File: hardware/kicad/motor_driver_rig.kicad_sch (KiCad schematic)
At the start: 8 parts, among them M1 NEMA-17 stepper motor, M2 NEMA-17 stepper motor, M3 NEMA-17 stepper motor, U1 Arduino Uno + CNC Shield V3

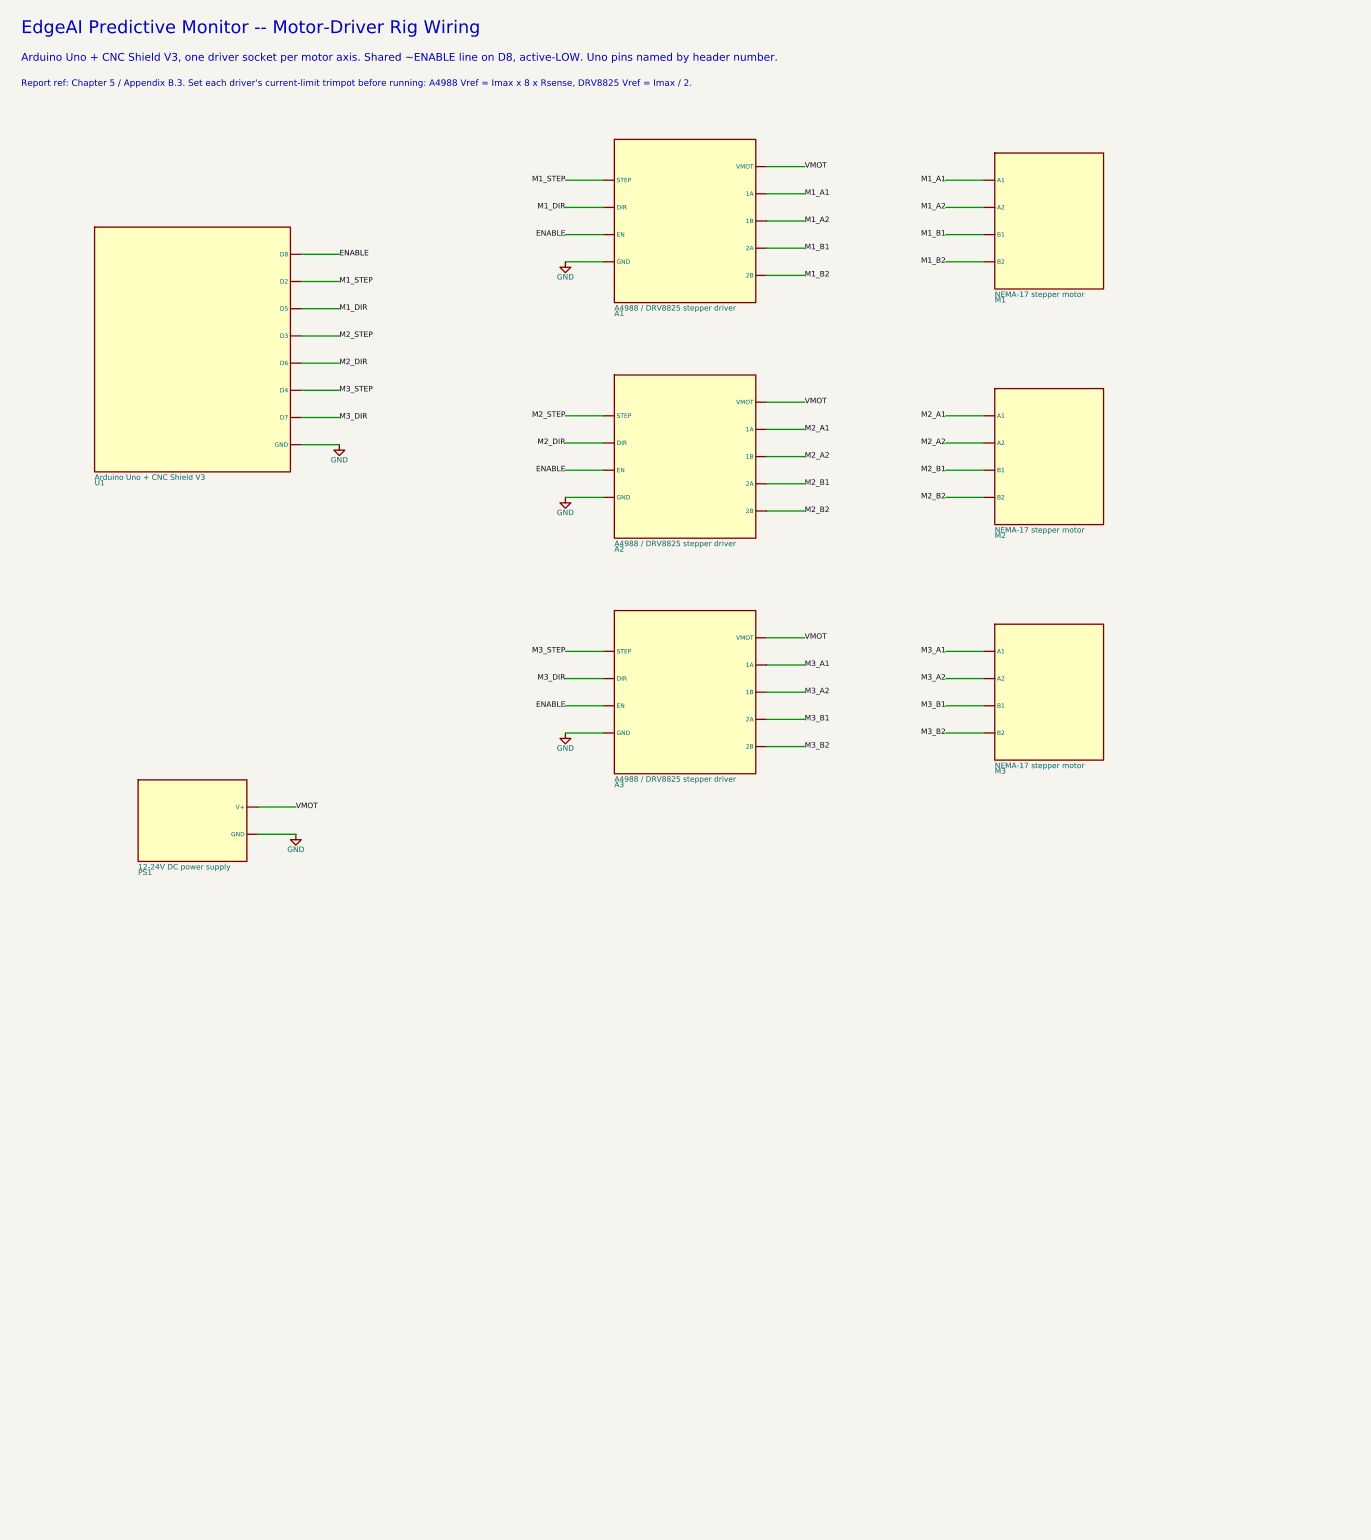
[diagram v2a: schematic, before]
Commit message: schematics: drop report-ref line, enlarge text, tighten crop
The report ref (Chapter/Appendix) was tied to a report structure the
submitted template doesn't use, so it's gone -- the useful pin-naming
and trimpot notes it was bundled with stayed. Separately, headings,
pin names, and net labels were too small to read once pasted into a
Word doc, so all text sizes went up in gen.py; row spacing now derives
from each part's real box height (via a new stack_column() helper)
instead of fixed y-coordinates, since the bigger fonts no longer fit
the old hand-picked positions. Crop step now masks out just the
title-block corner instead of scanning a fixed window, which cuts the
white margin around each exported PNG/PDF down to ~25px.

Co-Authored-By: Claude Sonnet 5 <noreply@anthropic.com>
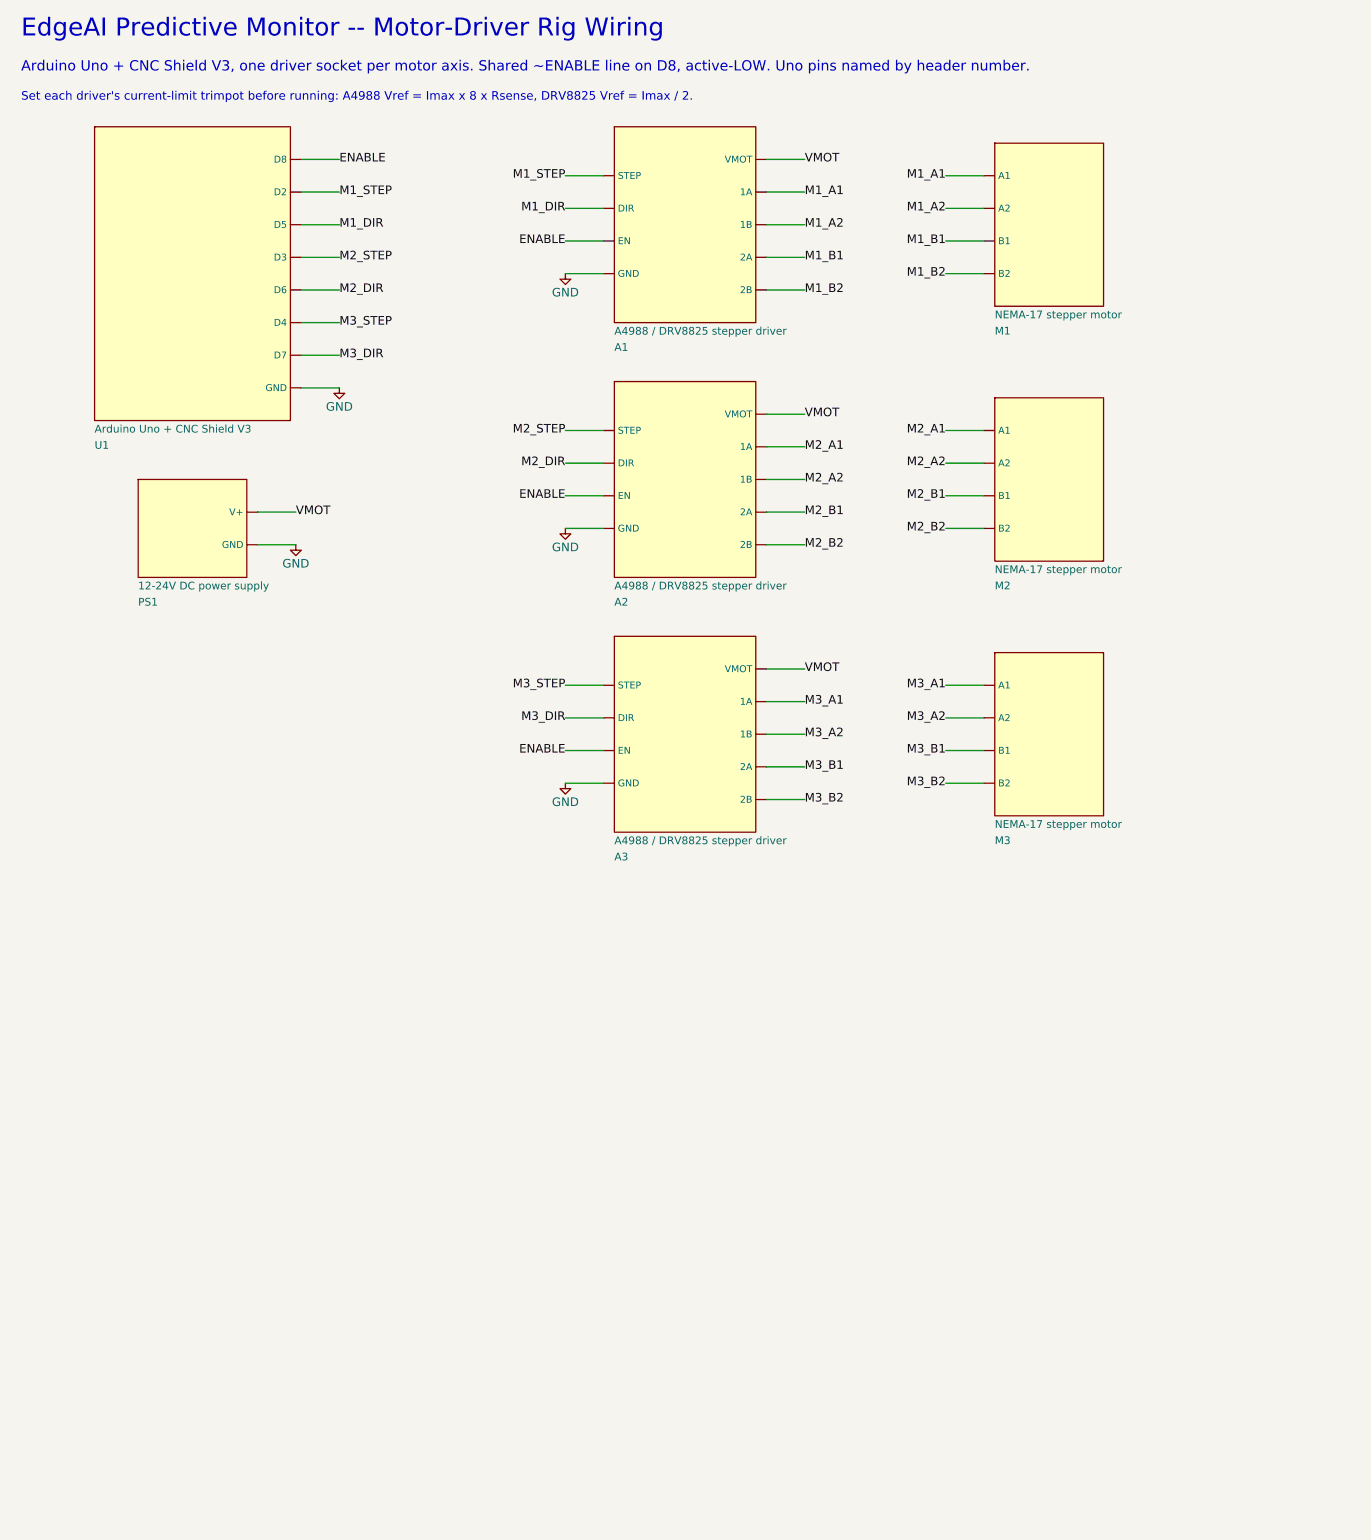
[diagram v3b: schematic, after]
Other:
- note added: "Set each driver's current-limit trimpot before running: A4988 Vref = Imax x 8 x Rsense, DRV8825 Vref = Imax / 2."
- note removed: "Report ref: Chapter 5 / Appendix B.3. Set each driver's current-limit trimpot before running: A4988 Vref = Imax x 8 x Rsense, DRV8825 Vref = Imax / 2."

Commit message: schematics: rework motor-driver rig to 2 columns, shorten subtitle
3 side-by-side columns (hub, driver, motor) squeezed to illegible
when pasted into Word, unlike the other two diagrams which are 2
columns. Driver and motor are now stacked per axis in a single right
column instead -- connectivity is unaffected since this style already
wires everything by matching net labels, not physical adjacency.
Also trimmed the subtitle, which at 134 chars had become the widest
line on the sheet and was stretching the crop past the actual circuit.

Co-Authored-By: Claude Sonnet 5 <noreply@anthropic.com>
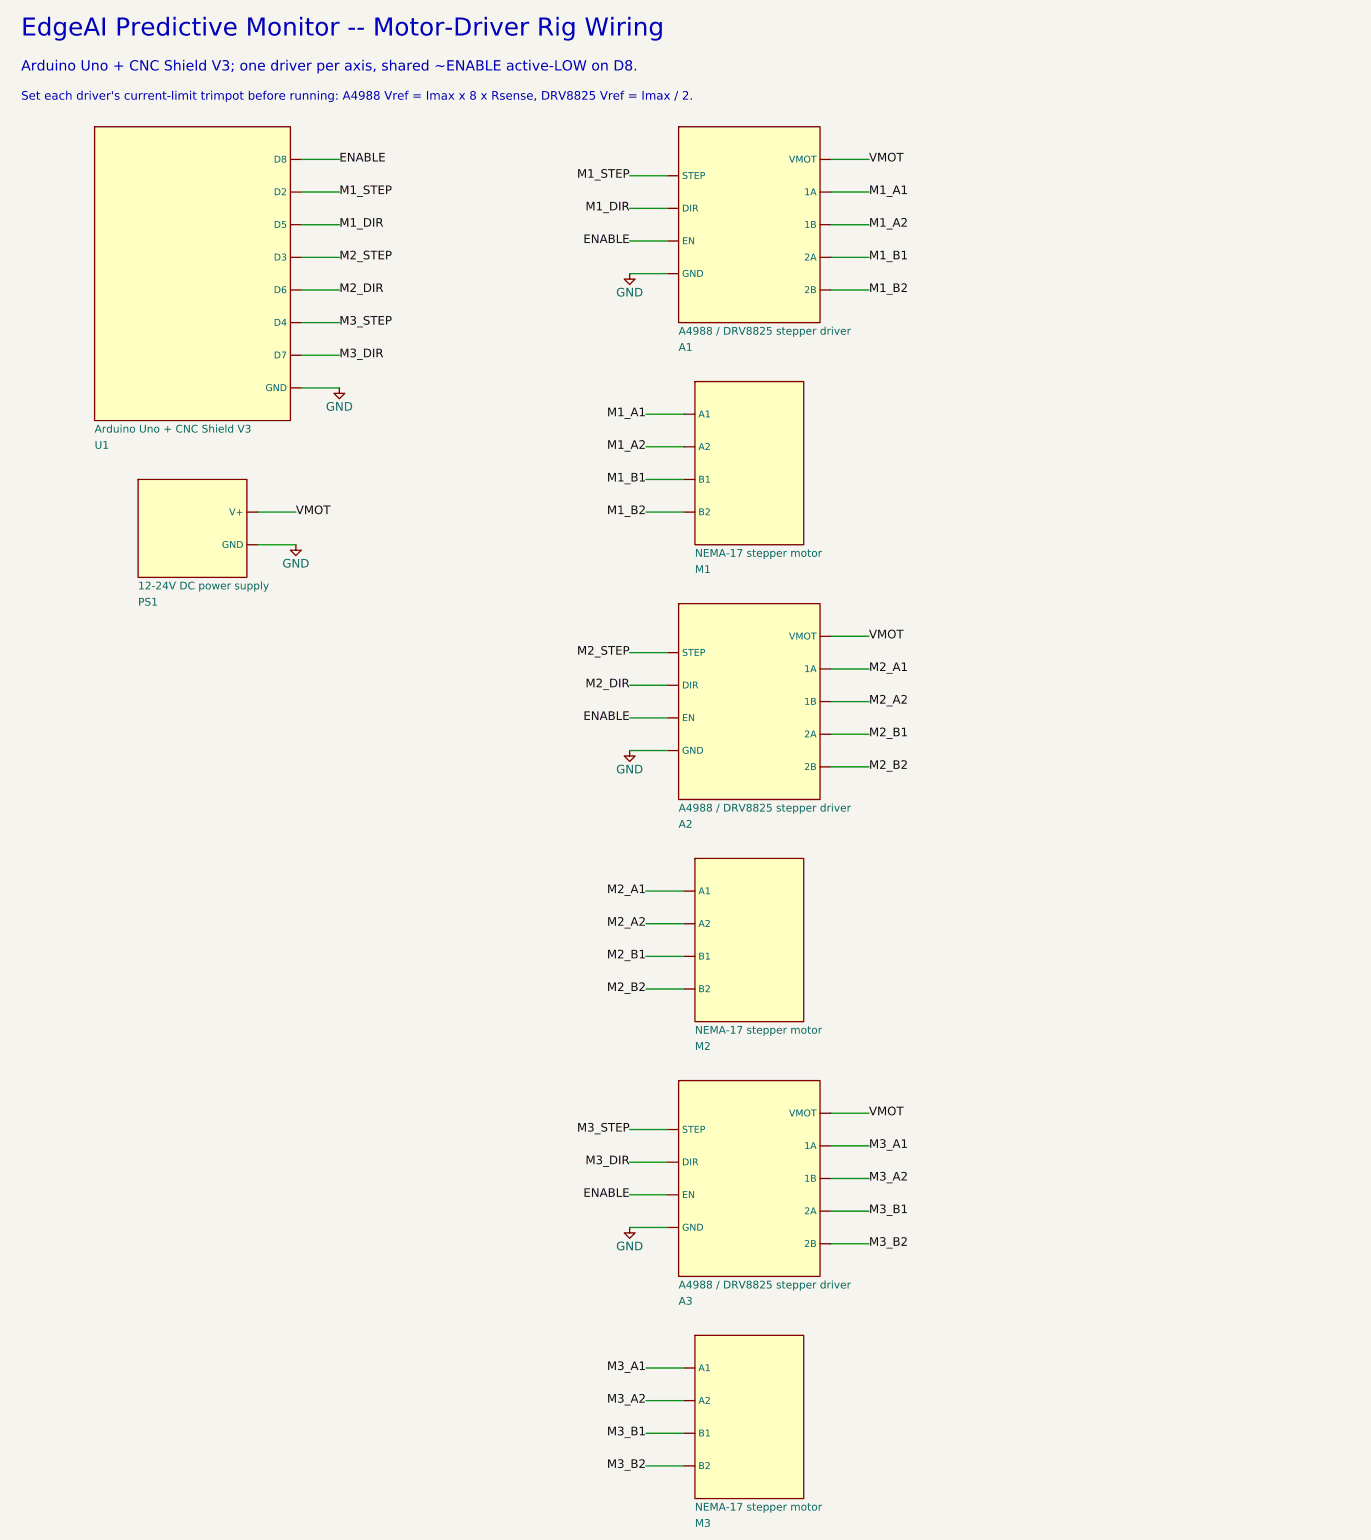
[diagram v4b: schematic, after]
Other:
- note added: "Arduino Uno + CNC Shield V3; one driver per axis, shared ~ENABLE active-LOW on D8."
- note removed: "Arduino Uno + CNC Shield V3, one driver socket per motor axis. Shared ~ENABLE line on D8, active-LOW. Uno pins named by header number."

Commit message: schematics: fix motor-driver rig layout to fill both columns, bottom cutoff
The previous 2-column pass stacked driver+motor per axis in a single
tall right column while the left column (hub+PSU) sat mostly empty --
6 rows deep, it also overflowed the A3 sheet height and got the M2/M3
row silently clipped by kicad-cli's page-bound raster export.

Now both columns carry rows: Uno + PSU share row 1, then each axis's
driver (col 1) and motor (col 2) share a row -- 4 rows instead of 6,
both columns filled, driver/motor labels still face each other across
the gap. Bumped the sheet to A2 for headroom against the same overflow
next time a part or row count grows; the auto-crop keeps the exported
image sized to content regardless, so this adds no visible whitespace.

Co-Authored-By: Claude Sonnet 5 <noreply@anthropic.com>
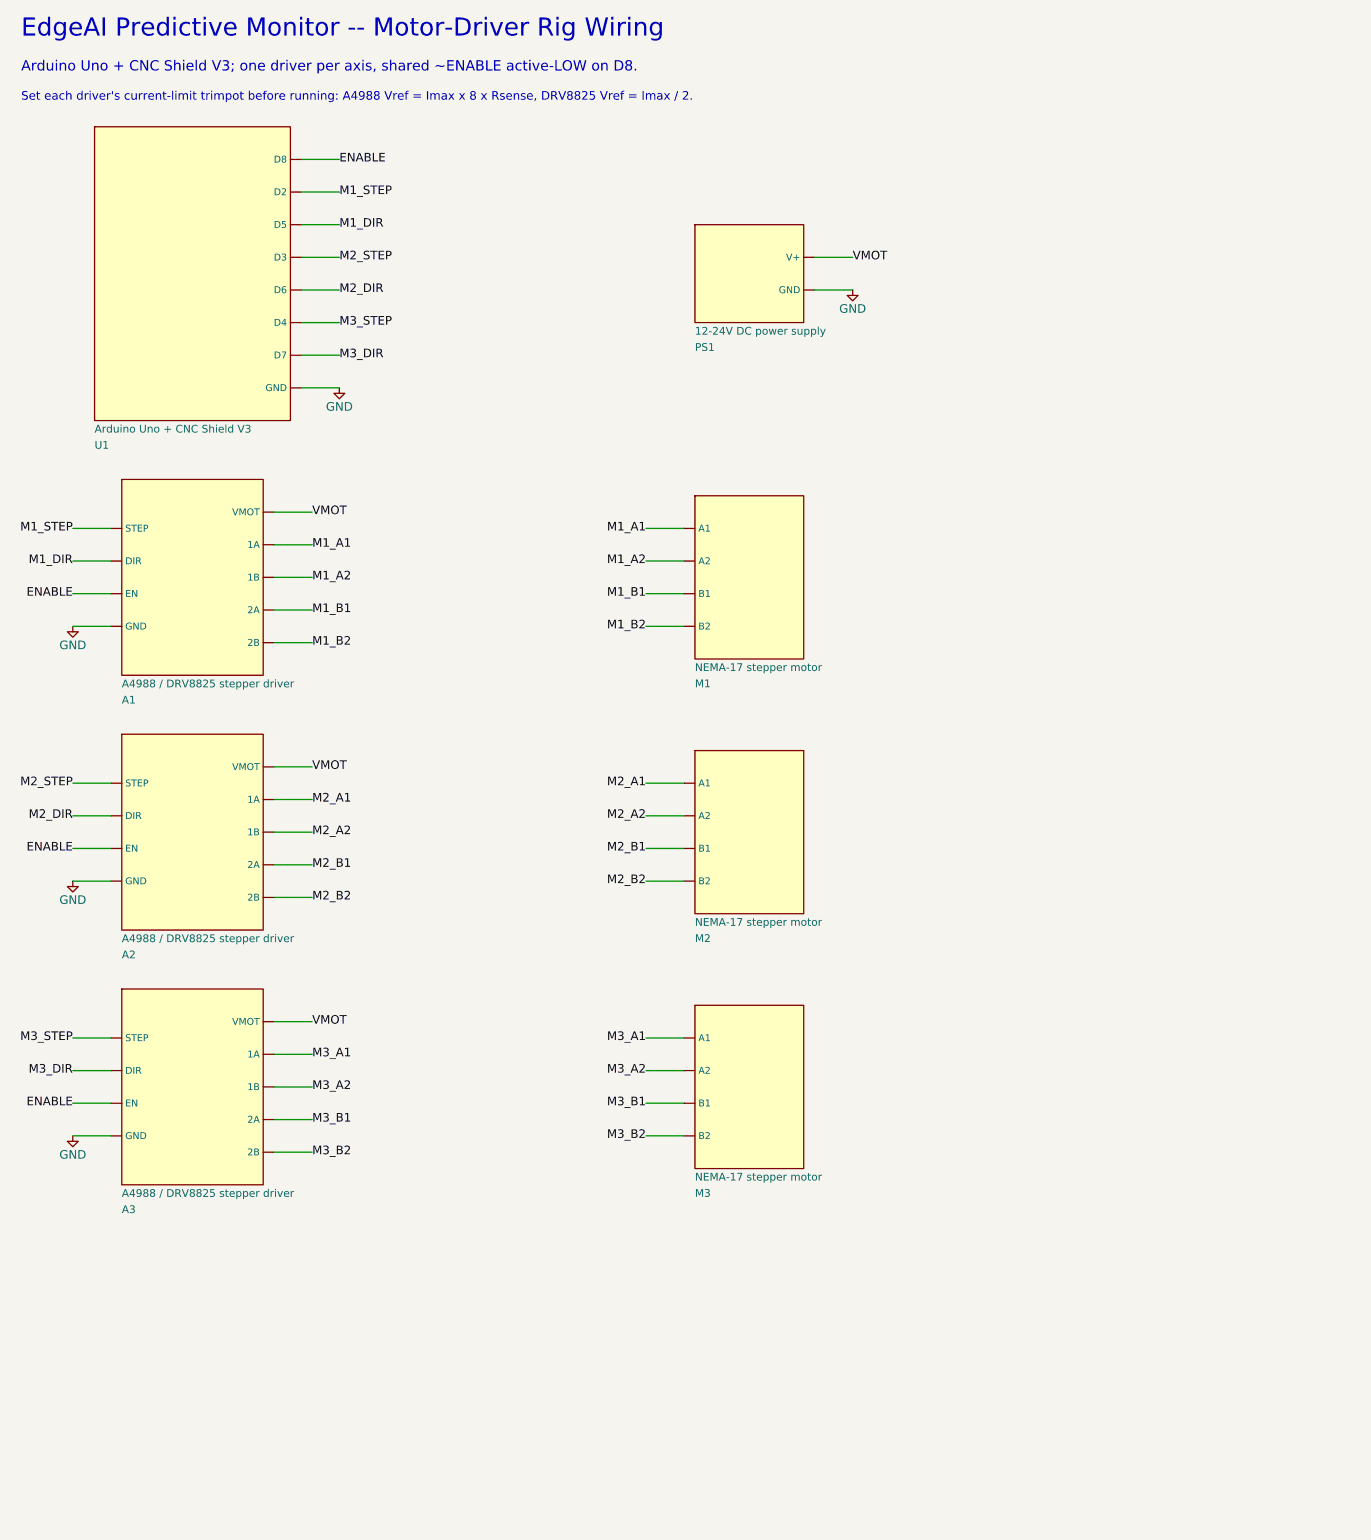
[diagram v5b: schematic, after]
